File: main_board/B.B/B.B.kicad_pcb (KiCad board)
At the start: 4 copper layers, 105 x 105 mm, 300 parts, among them J1 Conn_01x02, J2 Conn_01x08, J3 Conn_01x08, J4 AudioJack4, J5 USB_C_Receptacle_USB2.0, J6 USB_A, J7 SIM_Card, J8 Micro_SD_Card, M1 Motor_DC, Q1 CJ3134K, Q10 CJ3134K, Q11 Q_PMOS_DSG, Q12 CJ3134K, Q13 CJ3134K, Q14 CJ3134K, Q2 CJ3134K, Q3 CJ3134K, Q4 Q_NPN_BCE, Q5 Q_NPN_BCE, Q6 CJ3134K, Q7 Q_PMOS_DSG, Q8 CJ3134K, Q9 Q_PMOS_DSG, SW1 SW_DIP_x01, SW2 SW_DIP_x01, U1 WS2812, U10 WS2812, U11 WS2812, U12 WS2812, U13 WS2812, U14 WS2812, U15 WS2812, U16 WS2812, U17 WS2812, U18 WS2812, U19 WS2812, U2 WS2812, U20 WS2812, U21 WS2812, U22 WS2812, U23 WS2812, U24 WS2812, U25 WS2812, U26 WS2812, U27 WS2812, U28 WS2812, U29 WS2812, U3 WS2812, U30 WS2812, U31 WS2812, U32 WS2812, U33 WS2812, U34 WS2812, U35 WS2812, U36 WS2812, U37 WS2812, U38 WS2812, U39 WS2812, U4 WS2812, U40 WS2812, U41 WS2812, U42 WS2812, U43 WS2812, U44 WS2812, U45 WS2812, U46 WS2812, U47 WS2812, U48 WS2812, U49 WS2812, U5 WS2812, U50 WS2812, U51 WS2812, U52 WS2812, U53 WS2812, U54 WS2812, U55 WS2812, U56 WS2812, U57 WS2812, U58 WS2812, U59 WS2812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

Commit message: 18650
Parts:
- removed A9G1: A9G, BB:A9G
- removed AE1, AE2: Antenna_Shield, BB:conn_antena
- removed C100: 33nf, Capacitor_SMD:C_0402_1005Metric
- removed C101: 10pf, Capacitor_SMD:C_0402_1005Metric
- removed C113, C117, C118: 1uf, Resistor_SMD:R_0402_1005Metric
- removed C115: 10uf, Resistor_SMD:R_0805_2012Metric
- removed C116: 0.1uf, Resistor_SMD:R_0805_2012Metric
- removed C119: 4.7uf, Capacitor_SMD:C_0603_1608Metric
- removed C120: 1uf, Capacitor_SMD:C_0603_1608Metric
- removed C121: 100nf, Capacitor_SMD:C_0603_1608Metric
- removed C122, C123, C124, C125, C126, C127: 47pf, Capacitor_SMD:C_0402_1005Metric
- removed C128, C130: 22n, Capacitor_SMD:C_0402_1005Metric
- removed C129, C131: 18p/50V, Capacitor_SMD:C_0402_1005Metric
- removed C78, C79, C80, C81, C82, C83, C84: 0.1uf, Resistor_SMD:R_0402_1005Metric
- removed C86, C96: 2.2uf, Capacitor_SMD:C_0805_2012Metric
- removed C91, C95: 22uf, Capacitor_SMD:C_0805_2012Metric
- removed C94: 10uf, Resistor_SMD:R_0603_1608Metric
- removed C97: 100nf, Capacitor_SMD:C_0402_1005Metric
- removed C98: 1nf, Capacitor_SMD:C_0402_1005Metric
- removed C99: 1uf, Capacitor_SMD:C_0402_1005Metric
- removed D2: D_Schottky, BB:DO-214AC
- removed J1: Conn_01x02, Connector_PinHeader_2.54mm:PinHeader_1x02_P2.54mm_Vertical
- removed J4: AudioJack4, BB:JC-128
- removed J6: USB_A, BB:USBA-G-SMD
- removed J7: SIM_Card, BB:SIM
- removed J8: Micro_SD_Card, BB:micro-SD
- removed LS1, LS2, LS3: Speaker, Connector_PinHeader_2.54mm:PinHeader_1x02_P2.54mm_Vertical
- removed MK1, MK2, MK3: Microphone, Connector_PinHeader_2.54mm:PinHeader_1x02_P2.54mm_Vertical
- removed Q13, Q14: CJ3134K, Package_TO_SOT_SMD:SOT-23
- removed R51: 12k, Resistor_SMD:R_0402_1005Metric
- removed R52: 100k, Resistor_SMD:R_0402_1005Metric
- removed R53, R54: 47k, Resistor_SMD:R_0402_1005Metric
- removed U73: MH253ESO, Package_TO_SOT_SMD:SOT-23
- removed U74: WS2812, BB:WS2812
- removed e1: TPA2012D2, Package_DFN_QFN:QFN-20-1EP_4x4mm_P0.5mm_EP2.5x2.5mm
- added BT1: Battery_Cell, BB:18650-holder, B.Cu at (200.0, 100.0)
- added LED4: RED, LED_SMD:LED_0603_1608Metric, F.Cu at (245.8, 107.6)
- added LED5: BLUE, LED_SMD:LED_0603_1608Metric, F.Cu at (245.8, 103.5)
- added MMBT1: Q_NPN_BCE, Package_TO_SOT_SMD:SOT-23, F.Cu at (169.9, 89.5)
- added MMBT3904: Q_NPN_BCE, Package_TO_SOT_SMD:SOT-23, F.Cu at (173.7, 89.5)
- added R48: 1,2k, Resistor_SMD:R_0402_1005Metric, F.Cu at (244.0, 105.6)
- added SW3: SW_DIP_x01, Button_Switch_SMD:SW_Push_1P1T_NO_CK_KSC6xxJ, F.Cu at (223.8, 108.0)
- added SW4: SW_DIP_x02, BB:SW-SMD-4, F.Cu at (165.2, 100.0)
- C61: value 10uf -> 1uf; footprint Resistor_SMD:R_0603_1608Metric -> Capacitor_SMD:C_0402_1005Metric
- C62: value 10uf -> 2.2uf; footprint Resistor_SMD:R_0603_1608Metric -> Capacitor_SMD:C_0805_2012Metric
- C63, C64: value 1uf -> 10nf; footprint Resistor_SMD:R_0402_1005Metric -> Capacitor_SMD:C_0402_1005Metric
- C65: value 1uf -> 0.1uf
- C66: footprint Resistor_SMD:R_0402_1005Metric -> Capacitor_SMD:C_0402_1005Metric
- C67: value 0.1uf -> 10uf; footprint Resistor_SMD:R_0402_1005Metric -> Resistor_SMD:R_0805_2012Metric
- C68: footprint Resistor_SMD:R_0402_1005Metric -> Resistor_SMD:R_0805_2012Metric
- C69, C70, C77: value 0.1uf -> 1uf
- C71, C73: value 0.1uf -> 22n; footprint Resistor_SMD:R_0402_1005Metric -> Capacitor_SMD:C_0402_1005Metric
- C72: value 1uf -> 18p/50V; footprint Resistor_SMD:R_0402_1005Metric -> Capacitor_SMD:C_0402_1005Metric
- C74: value 0.1uf -> 18p/50V; footprint Resistor_SMD:R_0402_1005Metric -> Capacitor_SMD:C_0402_1005Metric
- C75: value 0.1uf -> 22uf; footprint Resistor_SMD:R_0402_1005Metric -> Capacitor_SMD:C_0805_2012Metric
- D1, D3: value D_Schottky -> SS54
- J2, J3: value Conn_01x08 -> Conn_01x10; footprint Connector_PinHeader_2.54mm:PinHeader_1x08_P2.54mm_Vertical -> Connector_PinHeader_2.54mm:PinHeader_1x10_P2.54mm_Vertical
- J5, U65: moved to F.Cu
- L1: footprint BB:SMD-PIND-10.5x11.5x4_2.5x3.0 -> BB:MWSA0603_6.6x7.1x3.0
- L2: value 3.3uH -> 2.2uH; footprint BB:SMD-PIND-12.8x13.5x5_2.0x5.0 -> BB:MWSA0603_6.6x7.1x3.0
- LED1, LED2: value LED -> RED
- LED3: value LED -> IR; footprint Diode_SMD:D_0402_1005Metric -> LED_SMD:LED_0603_1608Metric
- Q1, Q10, Q12, Q2, Q6, Q8: value CJ3134K -> 2N7002
- Q11, Q7, Q9: value Q_PMOS_DSG -> SI3447CDV
- Q3: value CJ3134K -> AO3400A
- Q4, Q5: value Q_NPN_BCE -> SI3447CDV; footprint Package_TO_SOT_SMD:SOT-23 -> BB:TSOP-6_1.5x3.0x0.95P
- R11: value 33k -> 47k
- R12: value 7.5k -> 15k
- R13: value 10 -> 7.5k
- R14: value 100k -> 56k
- R15: value 1.5 -> 56k
- R16: value 33k -> 1,2k
- R17: value 100k -> 1M
- R19: value 7.5k -> 1,2k
- R39: value 12k -> 220
- R4: value 330k -> 300k
- R40: value 12k -> 7.5k
- R46, R47: value 220 -> 47k
- R49: value 100k -> 220
- R5, R6: value 1K -> 100k
- R7, R8: value 1K -> 1M
- R9: value 1K -> 220
- U60: value AIC1747-18GV5TR -> WS2812; footprint Package_TO_SOT_SMD:SOT-23-5 -> BB:WS2812
- U61: value TLV320AIC3101 -> BMX055; footprint Package_DFN_QFN:QFN-32-1EP_5x5mm_P0.5mm_EP3.45x3.45mm -> BB:LGA_4.5x3
- U63: value FP6296 -> FP6276; footprint BB:SOP-8+1_3.76x4.96mm_P1.27mm -> Package_SO:SOP-8_3.76x4.96mm_P1.27mm
- U67: value PCA9555D-Interface_Expansion -> M41T62; footprint Package_SO:SOIC-24W_7.5x15.4mm_P1.27mm -> Package_DFN_QFN:QFN-16-1EP_3x3mm_P0.5mm_EP1.7x1.7mm
- U69: value BMX055 -> SPL06; footprint BB:LGA_4.5x3 -> BB:SMD-8_2x2.5x0.65P
- U70: value M41T62 -> MH253ESO; footprint Package_DFN_QFN:QFN-16-1EP_3x3mm_P0.5mm_EP1.7x1.7mm -> Package_TO_SOT_SMD:SOT-23
- U71: value SPL06 -> MH253ESO; footprint BB:SMD-8_2x2.5x0.65P -> Package_TO_SOT_SMD:SOT-23
- U72: value MH253ESO -> SE9017; footprint Package_TO_SOT_SMD:SOT-23 -> Package_SO:SOP-8_3.76x4.96mm_P1.27mm
- moved C15 287.6 mm to (63.1, 96.6), turned to 84 degrees
- moved C17 281.0 mm to (63.2, 104.4), turned to 96 degrees
- moved C12 279.4 mm to (66.0, 85.4), turned to 66 degrees
- moved C18 278.0 mm to (63.9, 108.2), turned to 102 degrees
- moved U17 277.7 mm to (60.2, 104.2), turned to 6 degrees
- moved C16 275.8 mm to (63.0, 100.5), turned to 90 degrees
- moved C25 272.4 mm to (78.6, 130.2), turned to 144 degrees
- moved U19 271.5 mm to (62.0, 112.4), turned to 18 degrees
- moved C13 270.9 mm to (64.7, 89.0), turned to 72 degrees
- moved C27 267.6 mm to (85.4, 134.0), turned to 156 degrees
- moved C22 267.1 mm to (70.3, 122.1), turned to 126 degrees
- moved C14 267.0 mm to (63.7, 92.8), turned to 78 degrees
- moved U20 265.1 mm to (63.5, 116.3), turned to 24 degrees
- moved U27 264.7 mm to (83.7, 136.5), turned to 66 degrees
- moved C7 264.0 mm to (77.9, 70.3), turned to 36 degrees
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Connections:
- C105 pad 1: /ESP3200/5V_USB -> Net-(C105-Pad1)
- C106 pad 1: /ESP3200/5V_USB -> Net-(C106-Pad1)
- C61 pad 1: +3V3 -> Net-(C61-Pad1)
- C61 pad 2: GND -> Net-(C61-Pad2)
- C62 pad 1: +3V3 -> /ESP3200/IO5-up
- C63 pad 1: +3V3 -> /next-board00/3V3
- C64 pad 1: +3V3 -> /next-board00/3V3
- C65 pad 1: +3V3 -> /next-board00/3V3
- C66 pad 1: +3V3 -> GND
- C66 pad 2: GND -> /next-board00/3V3
- C69 pad 1: +3V3 -> Net-(C69-Pad1)
- C71 pad 1: Net-(C71-Pad1) -> +3V3
- C72 pad 1: Net-(C71-Pad1) -> /expanz00/ENC_OUT_0
- C73 pad 1: Net-(C73-Pad1) -> +3V3
- C74 pad 1: /audio00/MIC2R -> /expanz00/ENC_OUT_1
- C74 pad 2: /audio00/MIC2L -> GND
- C76 pad 1: +5V -> Net-(C76-Pad1)
- C77 pad 1: /audio00/RIGHT_ROM -> /ESP3200/5V_USB
- C77 pad 2: Net-(C77-Pad2) -> GND
- C87 pad 1: VCC -> Net-(C87-Pad1)
- C90 pad 1: VCC -> Net-(C87-Pad1)
- D4 pad 1: Net-(C117-Pad1) -> Net-(C69-Pad1)
- J2 pad 6: /expanz00/IO1_4 -> /ESP3200/IO21
- J2 pad 7: /ESP3200/IO13 -> /ESP3200/IO19
- J2 pad 8: /ESP3200/IO15-up -> /ESP3200/IO18
- L2 pad 1: VCC -> Net-(C87-Pad1)
- Q1 pad 1: /SHUTDOWN_3V3 -> /ESP3200/IO5-up
- Q1 pad 3: Net-(Q1-Pad3) -> Net-(C61-Pad1)
- Q10 pad 1: /expanz00/WS2812-power -> /ESP3200/IO12-down
- Q11 pad 1: +5V -> VCC
- Q11 pad 2: +5V -> VCC
- Q11 pad 4: Net-(J6-Pad1) -> Net-(C76-Pad1)
- Q11 pad 5: +5V -> VCC
- Q11 pad 6: +5V -> VCC
- Q12 pad 1: /expanz00/power-out -> /ESP3200/5V_USB
- Q2 pad 1: /SHUTDOWN_5V -> /ESP3200/IO14
- Q3 pad 1: /ESP3200/5V_USB -> Net-(C106-Pad1)
- Q4 pad 1: Net-(Q4-Pad1) -> VCC
- Q4 pad 2: /ESP3200/EN -> VCC
- Q4 pad 3: /ESP3200/RTS -> GND
- Q5 pad 1: Net-(Q5-Pad1) -> VCC
- Q5 pad 2: /expanz00/INT-PCA -> VCC
- Q5 pad 3: /ESP3200/DTR -> Net-(C61-Pad1)
- Q7 pad 3: Net-(Q7-Pad3) -> Net-(Q10-Pad3)
- Q8 pad 1: /expanz00/MOTOR -> /ESP3200/IO13
- Q8 pad 3: Net-(Q7-Pad3) -> Net-(Q8-Pad3)
- Q9 pad 3: Net-(Q10-Pad3) -> Net-(Q8-Pad3)
- R10 pad 1: Net-(Q1-Pad3) -> Net-(R10-Pad1)
- R10 pad 2: VCC -> Net-(C87-Pad1)
- R13 pad 1: +5V -> GND
- R13 pad 2: Net-(C97-Pad2) -> Net-(R13-Pad2)
- R14 pad 2: Net-(R14-Pad2) -> Net-(R13-Pad2)
- R15 pad 1: LX -> Net-(R15-Pad1)
- R15 pad 2: Net-(C98-Pad2) -> GND
- R16 pad 1: Net-(R14-Pad2) -> Net-(LED4-Pad1)
- R16 pad 2: GND -> Net-(R16-Pad2)
- R17 pad 1: GND -> Net-(Q11-Pad3)
- R17 pad 2: Net-(R17-Pad2) -> VCC
- R18 pad 1: Net-(Q2-Pad3) -> Net-(C87-Pad1)
- R18 pad 2: LX -> Net-(Q2-Pad3)
- R19 pad 1: Net-(C101-Pad2) -> Net-(R19-Pad1)
- R20 pad 1: /expanz00/INT-PCA -> /expanz00/ENC_OUT_1
- R23 pad 1: Net-(Q4-Pad1) -> Net-(MMBT3904-Pad2)
- R26 pad 2: Net-(R24-Pad2) -> Net-(R26-Pad2)
- R27 pad 2: Net-(R25-Pad2) -> Net-(R27-Pad2)
- R28 pad 1: /ESP3200/5V_USB -> Net-(C106-Pad1)
- R29 pad 1: Net-(Q5-Pad1) -> Net-(MMBT1-Pad2)
- R3 pad 2: /ESP3200/IO34 -> /ESP3200/IO39
- R33 pad 2: /expanz00/INT-PCA -> /expanz00/ENC_OUT_1
- R39 pad 1: /next-board00/3V3 -> Net-(R39-Pad1)
- R39 pad 2: /next-board00/WS2812 -> /ESP3200/IO22
- R4 pad 1: /ESP3200/IO34 -> /ESP3200/IO39
- R40 pad 1: /next-board00/5V -> /next-board00/WS281200/DIN
- R40 pad 2: /next-board00/WS281200/DIN -> /next-board00/5V
- R41 pad 2: Net-(Q7-Pad3) -> Net-(Q10-Pad3)
- R42 pad 2: Net-(Q10-Pad3) -> Net-(Q8-Pad3)
- R43 pad 2: /ESP3200/IO18 -> /ESP3200/IO2-down
- R45 pad 1: +5V -> /ESP3200/IO27
- R45 pad 2: Net-(Q11-Pad3) -> GND
- R46 pad 1: Net-(R46-Pad1) -> +3V3
- R46 pad 2: /ESP3200/IO23 -> /expanz00/ENC_OUT_0
- R47 pad 1: Net-(R47-Pad1) -> +3V3
- R47 pad 2: /ESP3200/IO22 -> /expanz00/ENC_OUT_1
- R49 pad 1: /expanz00/perception00/int_baro -> /ESP3200/IO36
- R49 pad 2: GND -> Net-(C102-Pad1)
- R5 pad 1: /audio00/MICBIAS -> /ESP3200/IO13
- R5 pad 2: /audio00/MIC2L -> GND
- R6 pad 1: /audio00/MICBIAS -> Net-(C61-Pad1)
- R6 pad 2: Net-(C81-Pad1) -> VCC
- R7 pad 1: /audio00/MICBIAS -> Net-(C61-Pad2)
- R7 pad 2: Net-(C82-Pad1) -> Net-(C61-Pad1)
- R8 pad 1: Net-(C83-Pad1) -> /ESP3200/IO5-up
- R9 pad 1: Net-(C84-Pad1) -> Net-(R9-Pad1)
- R9 pad 2: GND -> /ESP3200/IO23
- U60 pad 1: +3V3 -> /next-board00/5V
- U60 pad 2: GND -> Net-(U60-Pad2)
- U60 pad 3: Net-(U60-Pad3) -> GND
- U60 pad 4: Net-(C73-Pad1) -> Net-(U59-Pad2)
- U61 pad 1: /ESP3200/IO33 -> /ESP3200/IO35
- U61 pad 10: /audio00/MIC1LP -> /ESP3200/IO25
- U61 pad 11: /audio00/MIC1LM -> /ESP3200/IO23
- U61 pad 12: /audio00/MIC1RP -> +3V3
- U61 pad 13: /audio00/MIC1RM -> +3V3
- U61 pad 14: /audio00/MIC2L -> /ESP3200/IO32
- U61 pad 15: /audio00/MICBIAS -> /ESP3200/IO33
- U61 pad 16: /audio00/MIC2R -> Net-(U61-Pad16)
- U61 pad 18: +3V3 -> (no net)
- U61 pad 19: /audio00/HPLOUT -> /ESP3200/IO34
- U61 pad 2: /audio00/BCLK -> Net-(U61-Pad2)
- U61 pad 20: Net-(U61-Pad20) -> +3V3
- U61 pad 3: /ESP3200/IO26 -> +3V3
- U61 pad 4: /audio00/DIN -> GND
- U61 pad 5: /audio00/DOUT -> Net-(U61-Pad5)
- U61 pad 8: /ESP3200/IO22 -> (no net)
- U61 pad 9: /ESP3200/IO23 -> /ESP3200/IO22
- U62 pad 4: Net-(Q1-Pad3) -> Net-(R10-Pad1)
- U62 pad 5: VCC -> Net-(C87-Pad1)
- U63 pad 3: Net-(C99-Pad2) -> Net-(C87-Pad1)
- U63 pad 5: Net-(R14-Pad2) -> GND
- U63 pad 6: Net-(C101-Pad2) -> Net-(R13-Pad2)
- U63 pad 7: Net-(R17-Pad2) -> Net-(R15-Pad1)
- U63 pad 8: Net-(C97-Pad2) -> +5V
- U64 pad 18: Net-(U64-Pad18) -> Net-(R26-Pad2)
- U64 pad 19: Net-(U64-Pad19) -> Net-(R27-Pad2)
- U64 pad 8: /ESP3200/5V_USB -> Net-(C106-Pad1)
- U65 pad 10: /audio00/BCLK -> /ESP3200/IO25
- U65 pad 12: /audio00/DIN -> /ESP3200/IO27
- U65 pad 13: /audio00/DOUT -> /ESP3200/IO14
- U65 pad 25: /expanz00/INT-PCA -> /expanz00/ENC_OUT_1
- U65 pad 26: /ESP3200/IO4 -> /expanz00/ENC_OUT_0
- U65 pad 4: /expanz00/ENC_OUT_1 -> /ESP3200/IO36
- U65 pad 8: /expanz00/ENC_OUT_0 -> /ESP3200/IO32
- U67 pad 1: /expanz00/INT-PCA -> Net-(U67-Pad1)
- U67 pad 10: /expanz00/perception00/int_baro -> Net-(R39-Pad1)
- U67 pad 11: /expanz00/sheet5F9AAC52/INT -> /ESP3200/IO26
- U67 pad 12: GND -> (no net)
- U67 pad 13: /expanz00/sheet5F9AAC52/RESET -> (no net)
- U67 pad 14: /expanz00/sheet5F9AAC52/PWR_KEY -> Net-(C69-Pad1)
- U67 pad 15: /expanz00/WS2812-power -> (no net)
- U67 pad 16: /expanz00/power-out -> (no net)
- U67 pad 17: /expanz00/IO1_4 -> (no net)
- U67 pad 2: GND -> Net-(U67-Pad2)
- U67 pad 4: /expanz00/perception00/int_accel1 -> Net-(U67-Pad4)
- U67 pad 5: /expanz00/perception00/int_accel2 -> GND
- U67 pad 6: /expanz00/perception00/int_giro1 -> (no net)
- U67 pad 7: /expanz00/perception00/int_giro2 -> (no net)
- U67 pad 8: /expanz00/perception00/int_magnet -> (no net)
- U67 pad 9: /expanz00/perception00/int_RTC -> Net-(R9-Pad1)
- U68 pad 3: /ESP3200/IO5-up -> /ESP3200/IO15-up
- U69 pad 1: /expanz00/perception00/int_accel2 -> GND
- U69 pad 3: +3V3 -> /ESP3200/IO23
- U69 pad 4: GND -> /ESP3200/IO22
- U69 pad 5: Net-(U69-Pad5) -> /ESP3200/IO27
- U69 pad 6: GND -> +3V3
- U69 pad 7: +3V3 -> GND
- U69 pad 8: (no net) -> +3V3
- U70 pad 1: Net-(U70-Pad1) -> +3V3
- U70 pad 2: Net-(U70-Pad2) -> /expanz00/ENC_OUT_0
- U71 pad 1: GND -> +3V3
- U71 pad 2: Net-(U71-Pad2) -> /expanz00/ENC_OUT_1
- U71 pad 3: /ESP3200/IO23 -> GND
- U72 pad 1: +3V3 -> /ESP3200/5V_USB
- U72 pad 2: /expanz00/ENC_OUT_0 -> (no net)
- Y1 pad 1: Net-(U70-Pad1) -> Net-(U67-Pad1)
- Y1 pad 2: Net-(U70-Pad2) -> Net-(U67-Pad2)
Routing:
- net /next-board00/5V: track 0.00 -> 284.2 mm, vias 0 -> 10
- net GND: track 0.00 -> 180.8 mm, vias 0 -> 64
- net /next-board00/3V3: track 0.00 -> 38.4 mm
- net /next-board00/SCL: track 0.00 -> 37.3 mm, vias 0 -> 1
- net /next-board00/SDA: track 0.00 -> 35.2 mm, vias 0 -> 1
- net /next-board00/SHUTDOWN: track 0.00 -> 29.5 mm, vias 0 -> 1
- net /next-board00/INT: track 0.00 -> 29.0 mm
- net /ESP3200/IO22: track 0.00 -> 12.4 mm
- net /ESP3200/IO23: track 0.00 -> 9.77 mm
- net /ESP3200/D-: track 0.00 -> 6.32 mm, vias 0 -> 2
- net /next-board00/WS2812: track 0.00 -> 5.97 mm
- net /next-board00/WS281200/DIN: track 0.00 -> 5.93 mm
- net Net-(U25-Pad2): track 0.00 -> 4.62 mm
- net /next-board00/WS281200/4-8: track 0.00 -> 4.62 mm
- net Net-(U55-Pad2): track 0.00 -> 4.62 mm
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- added copper zone on In1.Cu, net +5V
- added copper zone on F.Cu, net /next-board00/5V
- added copper zone on F.Cu, net GND
- added copper zone on B.Cu, net Net-(BT1-Pad1)
- added copper zone on F.Cu, net Net-(BT1-Pad1)
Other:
- board size 105 x 105 mm -> 196 x 98 mm

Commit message: PCB-0,1
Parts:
- removed Q12, Q6: 2N7002, Package_TO_SOT_SMD:SOT-23
- removed Q4: SI3447CDV, BB:TSOP-6_1.5x3.0x0.95P
- removed R17: 1M, Resistor_SMD:R_0402_1005Metric
- removed R40: 7.5k, Resistor_SMD:R_0402_1005Metric
- removed R44: 220, Resistor_SMD:R_0402_1005Metric
- added C78: 1000pf, Capacitor_SMD:C_0402_1005Metric, F.Cu at (89.0, 111.0)
- added C79: 1000pf, Capacitor_SMD:C_0402_1005Metric, F.Cu at (111.0, 111.0)
- added C80: 1000pf, Capacitor_SMD:C_0402_1005Metric, F.Cu at (111.0, 89.0)
- added F1: Polyfuse, Inductor_SMD:L_1206_3216Metric, F.Cu at (241.3, 102.5)
- added F2: Polyfuse, Inductor_SMD:L_1206_3216Metric, F.Cu at (241.3, 99.5)
- added L3: L, BB:coil, F.Cu at (83.0, 83.0)
- added L4: L, BB:coil, F.Cu at (83.0, 117.0)
- added L5: L, BB:coil, F.Cu at (117.0, 117.0)
- added L6: L, BB:coil, F.Cu at (117.0, 83.0)
- C112: value C -> 1000pf
- J2, J3: value Conn_01x10 -> Conn_01x11; footprint Connector_PinHeader_2.54mm:PinHeader_1x10_P2.54mm_Vertical -> Connector_PinHeader_2.54mm:PinHeader_1x11_P2.54mm_Vertical
- R16, R19: value 1,2k -> 1k
- R31, R32: value 5k1 -> 5.1k
- R48: value 1,2k -> 2k
- R5: value 100k -> 1k
- U72: footprint Package_SO:SOP-8_3.76x4.96mm_P1.27mm -> Package_TO_SOT_SMD:SOT-23-6
- moved R48 21.5 mm to (243.7, 84.1), turned to 270 degrees
- moved C76 21.1 mm to (241.5, 90.3), turned to 270 degrees
- moved R5 20.1 mm to (207.7, 101.6)
- moved U72 19.5 mm to (242.6, 87.0)
- moved C70 18.2 mm to (183.5, 131.2)
- moved U69 18.2 mm to (182.0, 133.0)
- moved R25 16.7 mm to (183.7, 105.0), turned to 90 degrees
- moved R16 16.6 mm to (242.6, 90.3), turned to 90 degrees
- moved Q11 15.9 mm to (238.7, 96.7), turned to 270 degrees
- moved LED4 15.1 mm to (242.6, 92.8)
- moved R24 15.1 mm to (182.7, 105.0), turned to 90 degrees
- moved J2 14.4 mm to (185.6, 70.0), turned to 90 degrees
- moved R19 14.0 mm to (244.9, 90.3), turned to 270 degrees
- moved R23 13.4 mm to (179.3, 103.0), turned to 0 degrees
- moved C77 13.2 mm to (243.7, 95.2), turned to 270 degrees
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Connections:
- BT1 pad 3: Net-(BT1-Pad1) -> Net-(BT1-Pad3)
- C1 pad 1: GND -> /next-board00/GND
- C10 pad 1: GND -> /next-board00/GND
- C106 pad 1: Net-(C106-Pad1) -> Net-(C105-Pad1)
- C11 pad 1: GND -> /next-board00/GND
- C12 pad 1: GND -> /next-board00/GND
- C13 pad 1: GND -> /next-board00/GND
- C14 pad 1: GND -> /next-board00/GND
- C15 pad 1: GND -> /next-board00/GND
- C16 pad 1: GND -> /next-board00/GND
- C17 pad 1: GND -> /next-board00/GND
- C18 pad 1: GND -> /next-board00/GND
- C19 pad 1: GND -> /next-board00/GND
- C2 pad 1: GND -> /next-board00/GND
- C20 pad 1: GND -> /next-board00/GND
- C21 pad 1: GND -> /next-board00/GND
- C22 pad 1: GND -> /next-board00/GND
- C23 pad 1: GND -> /next-board00/GND
- C24 pad 1: GND -> /next-board00/GND
- C25 pad 1: GND -> /next-board00/GND
- C26 pad 1: GND -> /next-board00/GND
- C27 pad 1: GND -> /next-board00/GND
- C28 pad 1: GND -> /next-board00/GND
- C29 pad 1: GND -> /next-board00/GND
- C3 pad 1: GND -> /next-board00/GND
- C30 pad 1: GND -> /next-board00/GND
- C31 pad 1: GND -> /next-board00/GND
- C32 pad 1: GND -> /next-board00/GND
- C33 pad 1: GND -> /next-board00/GND
- C34 pad 1: GND -> /next-board00/GND
- C35 pad 1: GND -> /next-board00/GND
- C36 pad 1: GND -> /next-board00/GND
- C37 pad 1: GND -> /next-board00/GND
- C38 pad 1: GND -> /next-board00/GND
- C39 pad 1: GND -> /next-board00/GND
- C4 pad 1: GND -> /next-board00/GND
- C40 pad 1: GND -> /next-board00/GND
- C41 pad 1: GND -> /next-board00/GND
- C42 pad 1: GND -> /next-board00/GND
- C43 pad 1: GND -> /next-board00/GND
- C44 pad 1: GND -> /next-board00/GND
- C45 pad 1: GND -> /next-board00/GND
- C46 pad 1: GND -> /next-board00/GND
- C47 pad 1: GND -> /next-board00/GND
- C48 pad 1: GND -> /next-board00/GND
- C49 pad 1: GND -> /next-board00/GND
- C5 pad 1: GND -> /next-board00/GND
- C50 pad 1: GND -> /next-board00/GND
- C51 pad 1: GND -> /next-board00/GND
- C52 pad 1: GND -> /next-board00/GND
- C53 pad 1: GND -> /next-board00/GND
- C54 pad 1: GND -> /next-board00/GND
- C55 pad 1: GND -> /next-board00/GND
- C56 pad 1: GND -> /next-board00/GND
- C57 pad 1: GND -> /next-board00/GND
- C58 pad 1: GND -> /next-board00/GND
- C59 pad 1: GND -> /next-board00/GND
- C6 pad 1: GND -> /next-board00/GND
- C60 pad 1: GND -> /next-board00/GND
- C63 pad 2: GND -> /next-board00/LDC-GND
- C64 pad 2: GND -> /next-board00/LDC-GND
- C65 pad 2: GND -> /next-board00/LDC-GND
- C66 pad 1: GND -> /next-board00/LDC-GND
- C7 pad 1: GND -> /next-board00/GND
- C76 pad 1: Net-(C76-Pad1) -> /charger00/BAT
- C8 pad 1: GND -> /next-board00/GND
- C87 pad 1: Net-(C87-Pad1) -> /charger00/BAT
- C9 pad 1: GND -> /next-board00/GND
- C90 pad 1: Net-(C87-Pad1) -> /charger00/BAT
- J2 pad 1: /expanz00/5V-WS2812 -> GND
- J2 pad 10: GND -> /expanz00/5V-WS2812
- J2 pad 2: /expanz00/5V-WS2812 -> GND
- J2 pad 3: +3V3 -> /ESP3200/IO18
- J2 pad 6: /ESP3200/IO21 -> GND
- J2 pad 8: /ESP3200/IO18 -> /ESP3200/IO21
- J2 pad 9: GND -> +3V3
- J3 pad 10: GND -> /next-board00/GND
- J3 pad 4: /next-board00/SCL -> /next-board00/SHUTDOWN
- J3 pad 5: /next-board00/SDA -> /next-board00/INT
- J3 pad 6: /next-board00/INT -> /next-board00/LDC-GND
- J3 pad 7: /next-board00/SHUTDOWN -> /next-board00/SDA
- J3 pad 8: /next-board00/WS2812 -> /next-board00/SCL
- J3 pad 9: GND -> /next-board00/WS2812
- J5 pad S1: GND -> Net-(J5-PadS1)
- L2 pad 1: Net-(C87-Pad1) -> /charger00/BAT
- LED1 pad 1: GND -> Net-(LED1-Pad1)
- LED1 pad 2: Net-(LED1-Pad2) -> GND
- LED2 pad 1: GND -> Net-(LED2-Pad1)
- LED2 pad 2: Net-(LED2-Pad2) -> GND
- MMBT1 pad 3: /expanz00/ENC_OUT_1 -> /ESP3200/IO0-up
- Q11 pad 3: Net-(Q11-Pad3) -> GND
- Q11 pad 4: Net-(C76-Pad1) -> Net-(F1-Pad1)
- Q3 pad 1: Net-(C106-Pad1) -> Net-(C105-Pad1)
- Q5 pad 4: Net-(C87-Pad1) -> /charger00/BAT
- Q7 pad 1: VCC -> +5V
- Q7 pad 2: VCC -> +5V
- Q7 pad 5: VCC -> +5V
- Q7 pad 6: VCC -> +5V
- Q8 pad 1: /ESP3200/IO13 -> /ESP3200/IO0-up
- R10 pad 2: Net-(C87-Pad1) -> /charger00/BAT
- R18 pad 1: Net-(C87-Pad1) -> /charger00/BAT
- R20 pad 1: /expanz00/ENC_OUT_1 -> /ESP3200/IO0-up
- R26 pad 1: Net-(LED1-Pad2) -> Net-(LED1-Pad1)
- R27 pad 1: Net-(LED2-Pad2) -> Net-(LED2-Pad1)
- R28 pad 1: Net-(C106-Pad1) -> Net-(C105-Pad1)
- R3 pad 1: VCC -> /charger00/BAT
- R33 pad 2: /expanz00/ENC_OUT_1 -> /ESP3200/IO0-up
- R41 pad 1: VCC -> +5V
- R5 pad 1: /ESP3200/IO13 -> Net-(C114-Pad1)
- R5 pad 2: GND -> +5V
- SW4 pad 3: Net-(C106-Pad1) -> Net-(C105-Pad1)
- U1 pad 3: GND -> /next-board00/GND
- U1 pad 4: /next-board00/WS281200/DIN -> /next-board00/WS2812
- U10 pad 3: GND -> /next-board00/GND
- U11 pad 3: GND -> /next-board00/GND
- U12 pad 3: GND -> /next-board00/GND
- U13 pad 3: GND -> /next-board00/GND
- U14 pad 3: GND -> /next-board00/GND
- U15 pad 3: GND -> /next-board00/GND
- U16 pad 3: GND -> /next-board00/GND
- U17 pad 3: GND -> /next-board00/GND
- U18 pad 3: GND -> /next-board00/GND
- U19 pad 3: GND -> /next-board00/GND
- U2 pad 3: GND -> /next-board00/GND
- U20 pad 3: GND -> /next-board00/GND
- U21 pad 3: GND -> /next-board00/GND
- U22 pad 3: GND -> /next-board00/GND
- U23 pad 3: GND -> /next-board00/GND
- U24 pad 3: GND -> /next-board00/GND
- U25 pad 3: GND -> /next-board00/GND
- U26 pad 3: GND -> /next-board00/GND
- U27 pad 3: GND -> /next-board00/GND
- U28 pad 3: GND -> /next-board00/GND
- U29 pad 3: GND -> /next-board00/GND
- U3 pad 3: GND -> /next-board00/GND
- U30 pad 3: GND -> /next-board00/GND
- U31 pad 3: GND -> /next-board00/GND
- U32 pad 3: GND -> /next-board00/GND
- U33 pad 3: GND -> /next-board00/GND
- U34 pad 3: GND -> /next-board00/GND
- U35 pad 3: GND -> /next-board00/GND
- U36 pad 3: GND -> /next-board00/GND
- U37 pad 3: GND -> /next-board00/GND
- U38 pad 3: GND -> /next-board00/GND
- U39 pad 3: GND -> /next-board00/GND
- U4 pad 3: GND -> /next-board00/GND
- U40 pad 3: GND -> /next-board00/GND
- U41 pad 3: GND -> /next-board00/GND
- U42 pad 3: GND -> /next-board00/GND
- U43 pad 3: GND -> /next-board00/GND
- U44 pad 3: GND -> /next-board00/GND
- U45 pad 3: GND -> /next-board00/GND
- U46 pad 3: GND -> /next-board00/GND
- U47 pad 3: GND -> /next-board00/GND
- U48 pad 3: GND -> /next-board00/GND
- U49 pad 3: GND -> /next-board00/GND
- U5 pad 3: GND -> /next-board00/GND
- U50 pad 3: GND -> /next-board00/GND
- U51 pad 3: GND -> /next-board00/GND
- U52 pad 3: GND -> /next-board00/GND
- U53 pad 3: GND -> /next-board00/GND
- U54 pad 3: GND -> /next-board00/GND
- U55 pad 3: GND -> /next-board00/GND
- U56 pad 3: GND -> /next-board00/GND
- U57 pad 3: GND -> /next-board00/GND
- U58 pad 3: GND -> /next-board00/GND
- U59 pad 3: GND -> /next-board00/GND
- U6 pad 3: GND -> /next-board00/GND
- U60 pad 3: GND -> /next-board00/GND
- U62 pad 5: Net-(C87-Pad1) -> /charger00/BAT
- U63 pad 3: Net-(C87-Pad1) -> /charger00/BAT
- U64 pad 8: Net-(C106-Pad1) -> Net-(C105-Pad1)
- U65 pad 16: /ESP3200/IO13 -> /expanz00/ENC_OUT_1
- U65 pad 25: /expanz00/ENC_OUT_1 -> /ESP3200/IO0-up
- U66 pad 17: GND -> /next-board00/LDC-GND
- U66 pad 4: GND -> /next-board00/LDC-GND
- U66 pad 8: GND -> /next-board00/LDC-GND
- U7 pad 3: GND -> /next-board00/GND
- U72 pad 1: /ESP3200/5V_USB -> Net-(R16-Pad2)
- U72 pad 2: (no net) -> GND
- U72 pad 3: GND -> /charger00/BAT
- U72 pad 4: Net-(C76-Pad1) -> /ESP3200/5V_USB
- U72 pad 5: (no net) -> Net-(R19-Pad1)
- U72 pad 6: Net-(R16-Pad2) -> Net-(R48-Pad2)
- U8 pad 3: GND -> /next-board00/GND
- U9 pad 3: GND -> /next-board00/GND
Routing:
- net /next-board00/GND: track 0.00 -> 461.0 mm, vias 0 -> 60
- net /ESP3200/IO0-up: track 0.00 -> 120.7 mm, vias 0 -> 6
- net /ESP3200/5V_USB: track 3.61 -> 120.9 mm, vias 0 -> 6
- net GND: track 180.8 -> 68.7 mm, vias 64 -> 57
- net /expanz00/ENC_OUT_1: track 0.00 -> 94.2 mm, vias 0 -> 2
- net /ESP3200/IO23: track 9.77 -> 91.6 mm, vias 0 -> 4
- net /ESP3200/IO22: track 12.4 -> 89.3 mm, vias 0 -> 3
- net VCC: track 0.00 -> 70.5 mm, vias 0 -> 5
- net /ESP3200/IO21: track 0.00 -> 70.4 mm
- net /expanz00/ENC_OUT_0: track 0.00 -> 70.2 mm, vias 0 -> 2
- net /ESP3200/IO18: track 0.00 -> 68.4 mm
- net /ESP3200/IO19: track 0.00 -> 67.8 mm
- net /ESP3200/EN: track 0.00 -> 62.5 mm, vias 0 -> 2
- net /ESP3200/IO12-down: track 0.00 -> 59.4 mm, vias 0 -> 2
- net /ESP3200/IO14: track 0.00 -> 59.0 mm, vias 0 -> 2
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- added copper zone on F.Cu, net +3V3
- added copper zone on In2.Cu, net +3V3
- added copper zone on F.Cu, net +5V
- added copper zone on F.Cu, net /charger00/BAT
- added copper zone on F.Cu, net /expanz00/5V-WS2812
- added copper zone on In1.Cu, net /next-board00/5V
- added copper zone on F.Cu, net /next-board00/GND
- added copper zone on B.Cu, net GND
- added copper zone on In1.Cu, net GND
- added copper zone on F.Cu, net LX
- added copper zone on B.Cu, net Net-(BT1-Pad3)
- added copper zone on F.Cu, net Net-(BT1-Pad3)
- added copper zone on F.Cu, net Net-(F1-Pad1)
- added copper zone on F.Cu, net VCC
- removed copper zone on In1.Cu, net +5V
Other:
- outline, holes or cut-outs redrawn
- net class Default: clearance 0.2 -> 0.18
- rule trace_clearance: 0.2 -> 0.18

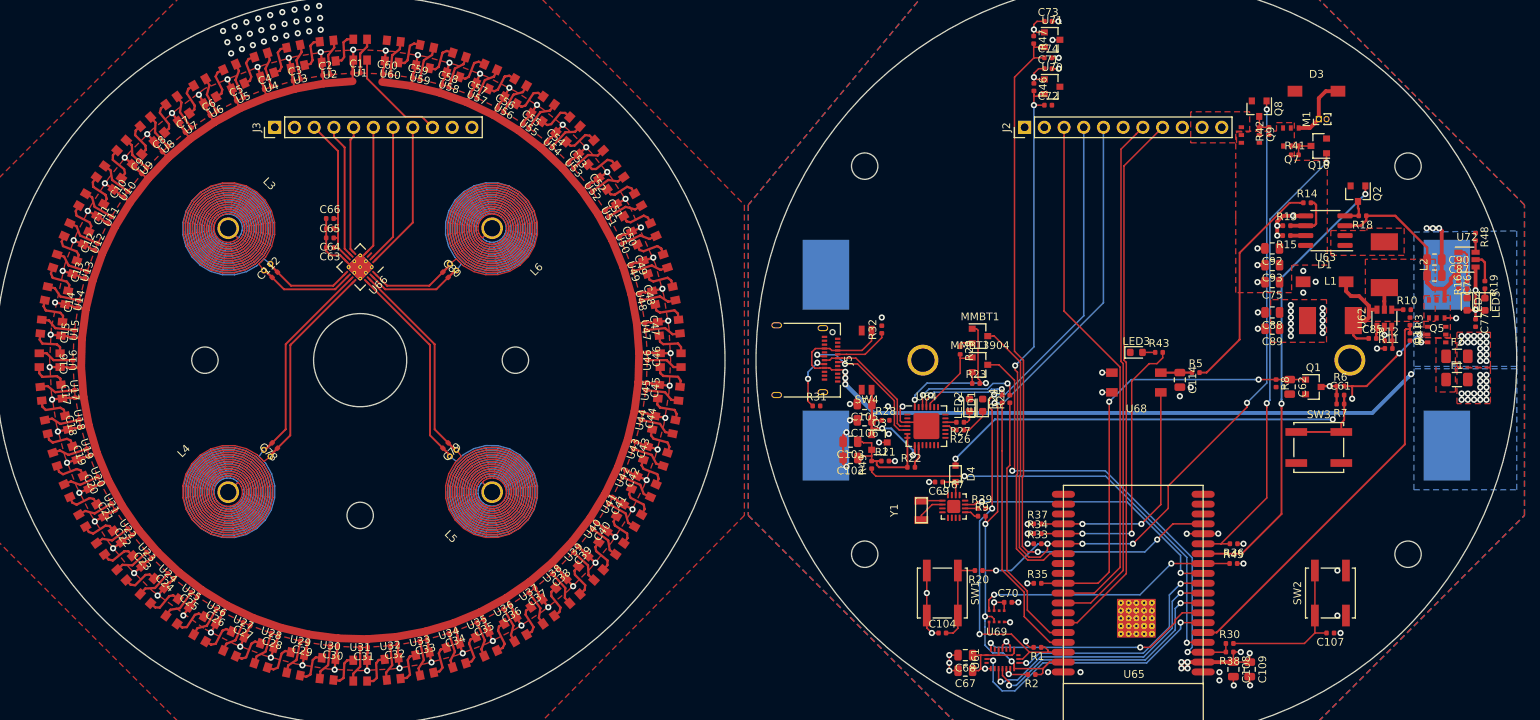
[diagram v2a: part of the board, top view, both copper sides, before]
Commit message: napajeni_na_stejne_strane
-poradi na konektoru
-napajeni IR prijmece z 5V na VCC
-vyssi nabijeci proud
-WS2812_power na IO21
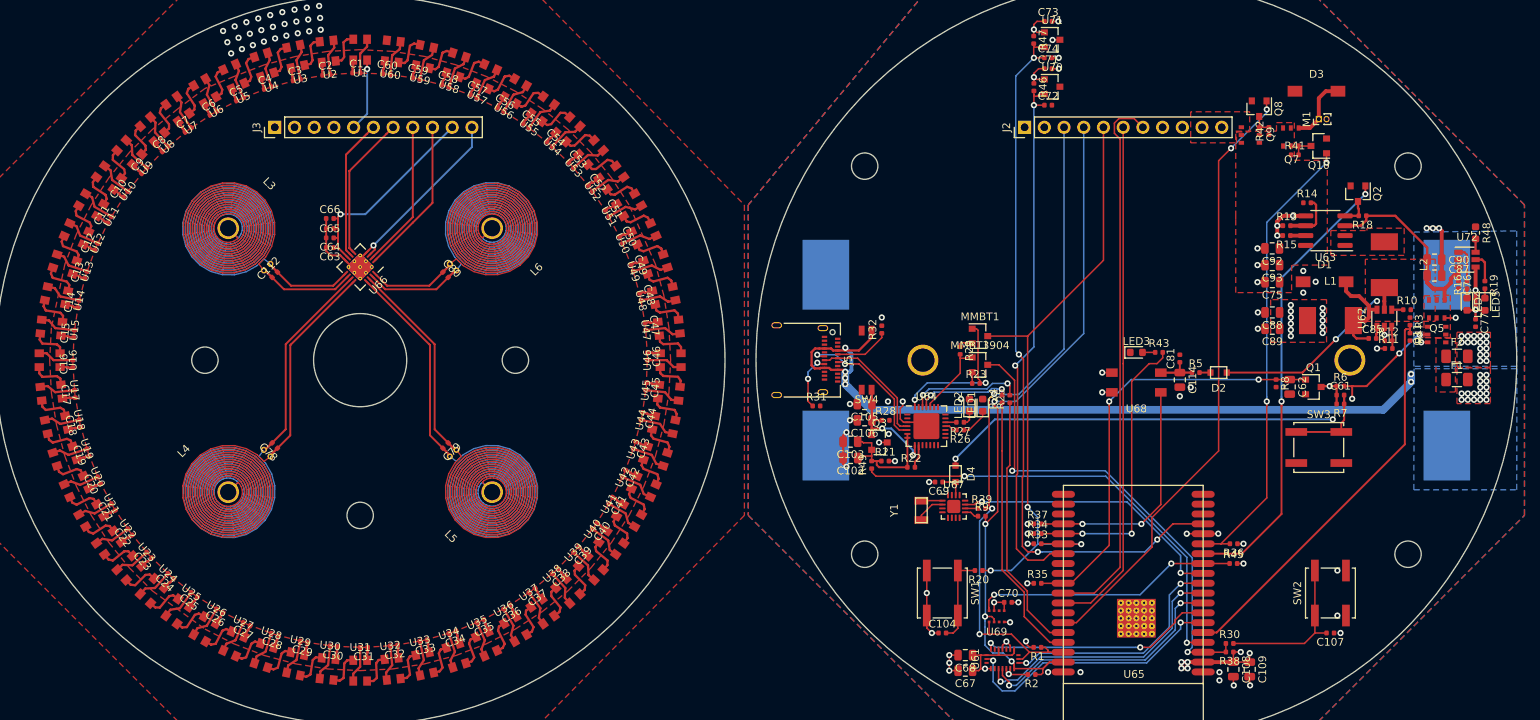
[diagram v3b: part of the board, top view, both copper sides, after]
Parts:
- added C81: 0.1uf, Resistor_SMD:R_0402_1005Metric, F.Cu at (205.6, 99.8)
- added D2: D, BB:SOD-323, F.Cu at (210.6, 101.6)
- R48: value 2k -> 1.5k; footprint Resistor_SMD:R_0402_1005Metric -> Resistor_SMD:R_0603_1608Metric
- moved R48 0.52 mm to (243.7, 83.6)
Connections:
- C76 pad 1: /charger00/BAT -> VCC
- C87 pad 1: /charger00/BAT -> VCC
- C90 pad 1: /charger00/BAT -> VCC
- D4 pad 2: VCC -> /BAT+
- J2 pad 2: GND -> +3V3
- J2 pad 3: /ESP3200/IO18 -> /ESP3200/IO22
- J2 pad 4: /ESP3200/IO22 -> /ESP3200/IO23
- J2 pad 5: /ESP3200/IO23 -> /ESP3200/IO0-up
- J2 pad 6: GND -> /ESP3200/IO19
- J2 pad 7: /ESP3200/IO19 -> /ESP3200/IO18
- J2 pad 8: /ESP3200/IO21 -> GND
- J2 pad 9: +3V3 -> GND
- J3 pad 10: /next-board00/GND -> /next-board00/3V3
- J3 pad 11: /next-board00/GND -> /next-board00/LDC-GND
- J3 pad 3: /next-board00/3V3 -> /next-board00/GND
- J3 pad 4: /next-board00/SHUTDOWN -> /next-board00/GND
- J3 pad 5: /next-board00/INT -> /next-board00/WS2812
- J3 pad 6: /next-board00/LDC-GND -> /next-board00/SHUTDOWN
- J3 pad 7: /next-board00/SDA -> /next-board00/INT
- J3 pad 8: /next-board00/SCL -> /next-board00/SDA
- J3 pad 9: /next-board00/WS2812 -> /next-board00/SCL
- L2 pad 1: /charger00/BAT -> VCC
- Q11 pad 1: VCC -> /BAT+
- Q11 pad 2: VCC -> /BAT+
- Q11 pad 5: VCC -> /BAT+
- Q11 pad 6: VCC -> /BAT+
- Q5 pad 1: VCC -> /BAT+
- Q5 pad 2: VCC -> /BAT+
- Q5 pad 4: /charger00/BAT -> VCC
- Q5 pad 5: VCC -> /BAT+
- Q5 pad 6: VCC -> /BAT+
- Q8 pad 1: /ESP3200/IO0-up -> /ESP3200/IO21
- R10 pad 2: /charger00/BAT -> VCC
- R18 pad 1: /charger00/BAT -> VCC
- R3 pad 1: /charger00/BAT -> VCC
- R5 pad 2: +5V -> Net-(D2-Pad1)
- R6 pad 2: VCC -> /BAT+
- U62 pad 5: /charger00/BAT -> VCC
- U63 pad 3: /charger00/BAT -> VCC
- U66 pad 3: Net-(U66-Pad3) -> /next-board00/LDC-GND
- U72 pad 3: /charger00/BAT -> VCC
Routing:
- net /next-board00/GND: track 461.0 -> 101.0 mm, vias 60 -> 0
- net /BAT+: track 0.00 -> 70.5 mm, vias 0 -> 5
- net /ESP3200/IO0-up: track 120.7 -> 82.7 mm, vias 6 -> 3
- net /charger00/BAT: track 31.9 -> 0.00 mm
- net +5V: track 29.0 -> 0.00 mm
- net VCC: track 70.5 -> 55.0 mm, vias 5 -> 2
- net /ESP3200/5V_USB: track 120.9 -> 130.5 mm, vias 6 -> 8
- net /ESP3200/IO21: track 70.4 -> 79.1 mm, vias 0 -> 2
- net /next-board00/LDC-GND: track 30.8 -> 37.6 mm, vias 0 -> 1
- net /next-board00/3V3: track 20.9 -> 27.5 mm, vias 0 -> 1
- net /next-board00/SHUTDOWN: track 17.4 -> 21.9 mm
- net /next-board00/WS2812: track 13.4 -> 9.38 mm, vias 0 -> 1
- net /next-board00/INT: track 16.4 -> 19.5 mm
- net /ESP3200/IO18: track 68.4 -> 70.6 mm
- net /ESP3200/IO5-up: track 57.8 -> 55.8 mm
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- added copper zone on F.Cu, net /BAT+
- removed copper zone on F.Cu, net /charger00/BAT

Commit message: lenky_k_CP2102
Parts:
- R5: value 1k -> 470
- moved LED1 0.20 mm to (180.0, 105.8)
- moved LED2 0.10 mm to (178.4, 105.8)
- moved R5 0.05 mm to (207.6, 101.6)
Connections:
- LED1 pad 2: GND -> Net-(C102-Pad1)
- LED2 pad 2: GND -> Net-(C102-Pad1)
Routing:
- net Net-(C102-Pad1): track 17.5 -> 36.4 mm
- net GND: vias 57 -> 56
